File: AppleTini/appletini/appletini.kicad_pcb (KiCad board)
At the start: 4 copper layers, 114.3 x 66.7 mm, 30 parts, among them J1 Conn_02x25_Counter_Clockwise, Q1 DMG2305UX-7, SW1 SW_Push, U1 74LS245, U2 74LS245, U3 74LS245, U4 74LS245, U5 74LS245, U6 74LS07, U7 Pico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

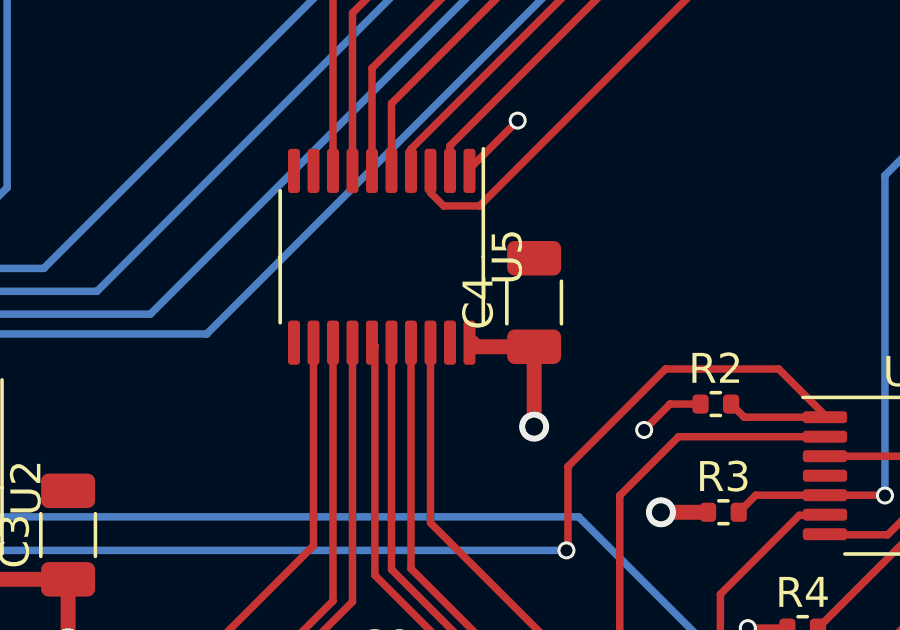
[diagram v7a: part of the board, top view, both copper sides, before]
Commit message: missing ground trace on U5
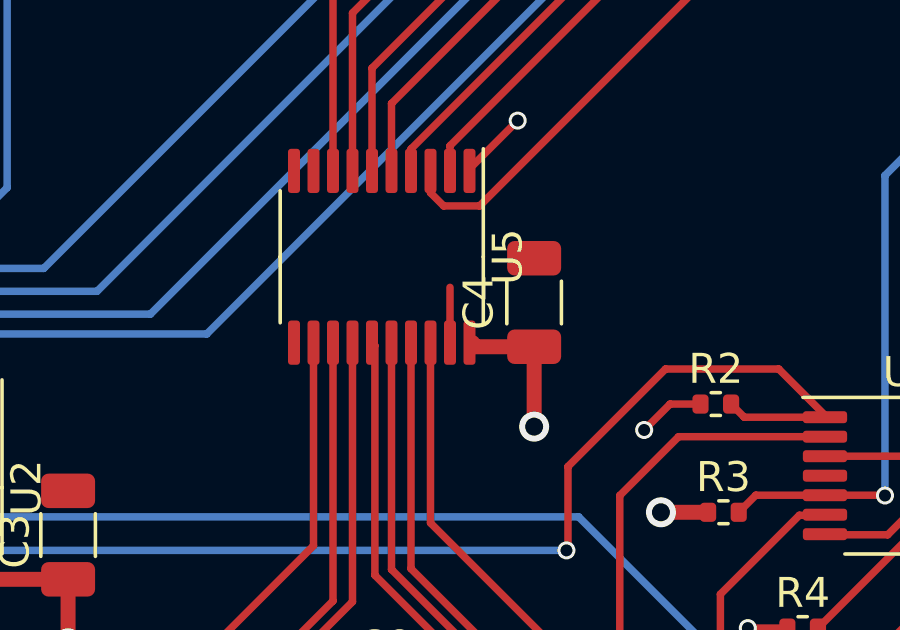
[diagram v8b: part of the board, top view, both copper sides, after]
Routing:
- net GND: track 39.1 -> 40.9 mm
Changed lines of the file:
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@@
   (via (at 173.7868 120.2436) (size 0.6) (drill 0.4) (layers "F.Cu" "B.Cu") (net 1))
   (via (at 140.208 120.65) (size 1) (drill 0.6) (layers "F.Cu" "B.Cu") (net 1))
+  (segment (start 163.86 110.7286) (end 163.86 108.8852) (width 0.25) (layer "F.Cu") (net 2))
   (segment (start 176.4634 114.5136) (end 176.4438 114.5332) (width 0.25) (layer "F.Cu") (net 2))
   (segment (start 163.1714 123.9502) (end 163.1714 122.682) (width 0.5) (layer "F.Cu") (net 2))
